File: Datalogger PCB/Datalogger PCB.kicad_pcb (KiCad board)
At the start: 4 copper layers, 42.2 x 101.8 mm, 51 parts, among them J1 Conn_01x02_Pin, M1 Motor_Servo, M2 Motor_Servo, M3 Motor_Servo, M4 Motor_Servo, U1 Teensy4.1, U2 BNO055, U3 LPS25HB, U4 AMS1117-5.0, U5 NRF24L01_Breakout, U6 VN5E160STR-E, U7 VN5E160STR-E, U8 VN5E160STR-E, U9 VN5E160STR-E

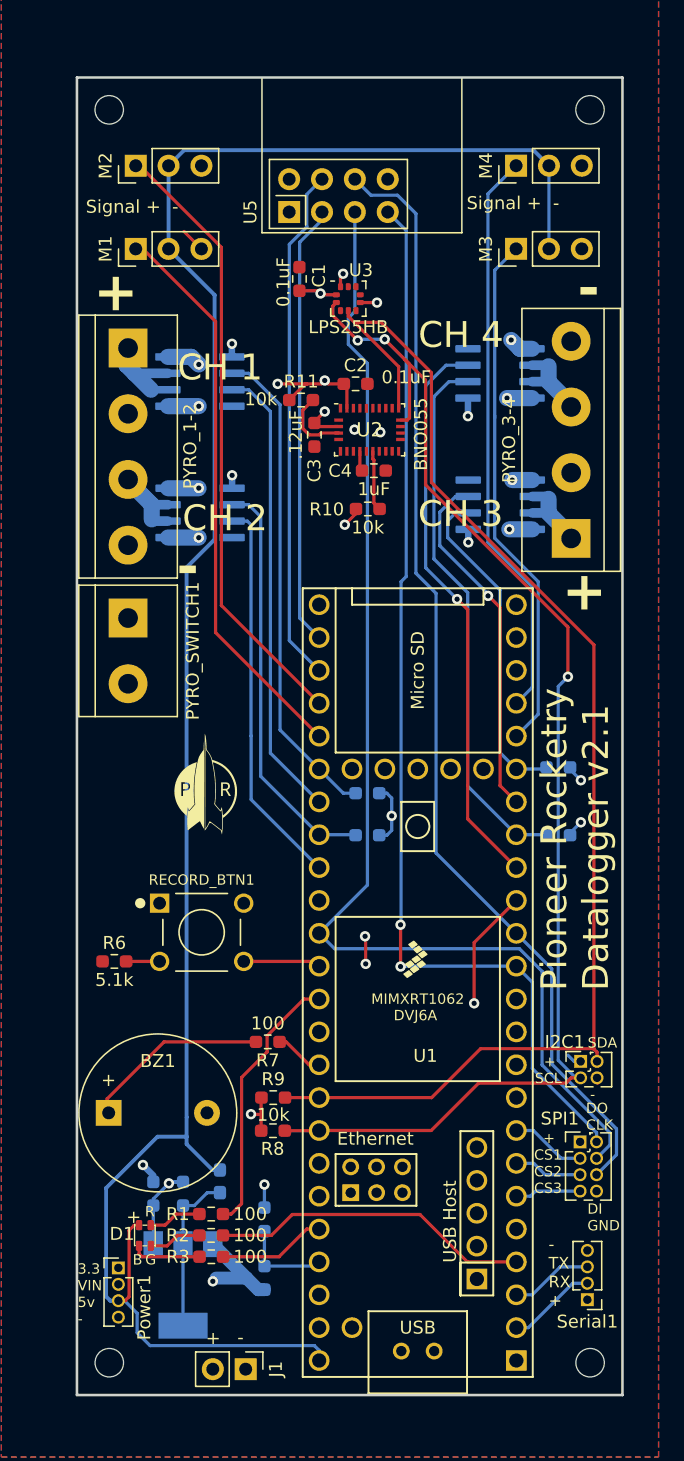
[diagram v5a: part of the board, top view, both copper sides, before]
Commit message: Made connectors bigger and removed unused radio connector
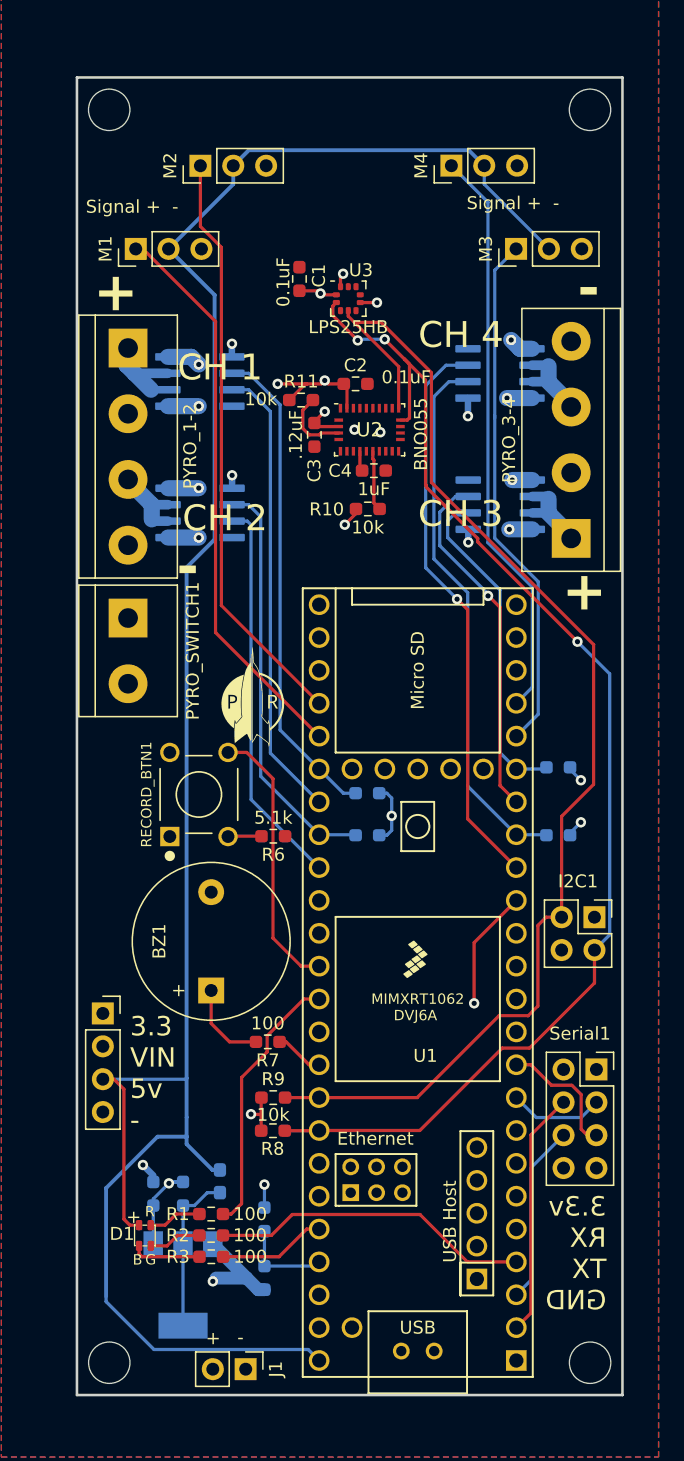
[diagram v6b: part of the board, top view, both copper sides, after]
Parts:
- removed SPI1: Conn_02x04_Counter_Clockwise, Connector_PinHeader_1.27mm:PinHeader_2x04_P1.27mm_Vertical
- removed U5: NRF24L01_Breakout, RF_Module:nRF24L01_Breakout
- H1, H2, H3, H4: footprint MountingHole:MountingHole_2.2mm_M2 -> MountingHole:MountingHole_3.2mm_M3
- I2C1: footprint Connector_PinHeader_1.27mm:PinHeader_2x02_P1.27mm_Vertical -> Connector_PinSocket_2.54mm:PinSocket_2x02_P2.54mm_Vertical
- Power1: footprint Connector_PinHeader_1.27mm:PinHeader_1x04_P1.27mm_Vertical -> Connector_PinSocket_2.54mm:PinSocket_1x04_P2.54mm_Vertical
- Serial1: value Conn_01x04_Pin -> Conn_02x04_Odd_Even; footprint Connector_PinHeader_1.27mm:PinHeader_1x04_P1.27mm_Vertical -> Connector_PinSocket_2.54mm:PinSocket_2x04_P2.54mm_Vertical
- moved Power1 19.7 mm to (139.6, 114.5)
- moved Serial1 17.8 mm to (177.7, 118.9), turned to 0 degrees
- moved R6 15.6 mm to (152.7, 100.8), turned to 180 degrees
- moved BZ1 12.3 mm to (147.9, 112.8), turned to 90 degrees
- moved I2C1 11.2 mm to (177.6, 107.1)
- moved RECORD_BTN1 10.7 mm to (147.0, 97.6), turned to 90 degrees
- moved G*** 7.68 mm to (151.1, 89.9)
- moved M2 5.00 mm to (147.1, 49.0)
- moved M4 5.00 mm to (166.5, 49.0)
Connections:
- Serial1 pad 2: /RX -> +3.3V
- Serial1 pad 3: /TX -> /RX2
- Serial1 pad 4: GND -> /RX
- U1 pad 10: unconnected-(U1-8_TX2_IN1-Pad10) -> /TX2
- U1 pad 26: /RADIO_CE -> unconnected-(U1-34_RX8-Pad26)
- U1 pad 27: /RADIO_CS -> unconnected-(U1-35_TX8-Pad27)
- U1 pad 9: unconnected-(U1-7_RX2_OUT1A-Pad9) -> /RX2
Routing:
- net /CLK: track 93.6 -> 0.00 mm
- net /DI: track 87.2 -> 0.00 mm
- net /DO: track 84.2 -> 0.00 mm, vias 2 -> 0
- net /RADIO_CS: track 40.0 -> 0.00 mm
- net /RADIO_CE: track 34.2 -> 0.00 mm
- net /RECORD_BTN: track 6.63 -> 21.8 mm
- net /RX: track 6.91 -> 18.9 mm
- net /TX2: track 0.00 -> 10.0 mm
- net Net-(BZ1--): track 14.4 -> 6.60 mm
- net /RX2: track 0.00 -> 7.79 mm
- net /TX: track 6.38 -> 13.8 mm
- net +5V: track 161.4 -> 167.2 mm
- net /EXTERNAL_CS1: track 5.82 -> 0.00 mm
- net /EXTERNAL_CS2: track 5.29 -> 0.00 mm
- net /EXTERNAL_CS3: track 5.09 -> 0.00 mm
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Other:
- board text added: "3.3v RX TX GND"
- board text removed: "+ CS1 CS2 CS3"
- board text removed: "+ SCL"
- board text removed: "- TX RX +"
- board text removed: "DI GND"
- board text removed: "DO CLK"
- board text removed: "SDA"

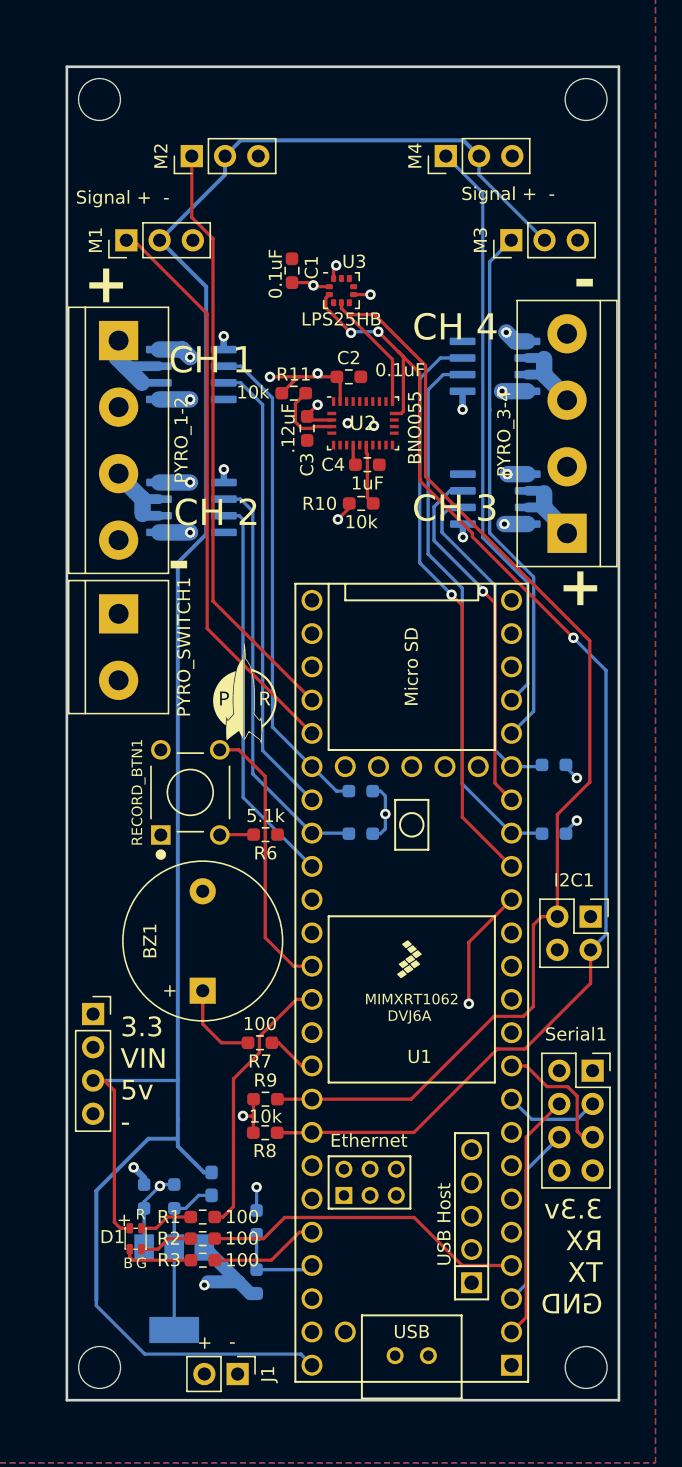
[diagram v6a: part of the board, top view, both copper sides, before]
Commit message: Removed Diode and replaced with jumper
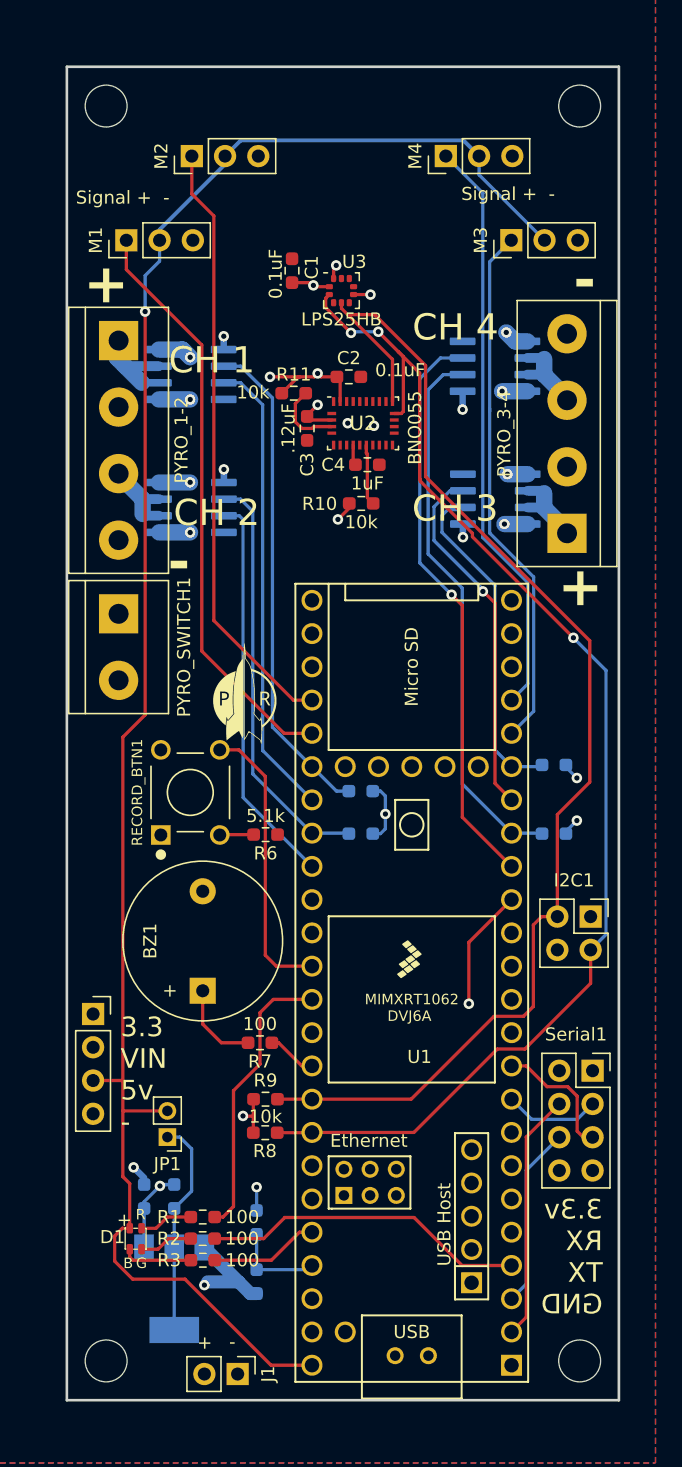
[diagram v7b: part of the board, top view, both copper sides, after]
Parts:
- removed D2: D, Diode_SMD:D_0603_1608Metric_Pad1.05x0.95mm_HandSolder
- added JP1: Jumper_2_Open, Connector_PinHeader_2.00mm:PinHeader_1x02_P2.00mm_Vertical, F.Cu at (145.2, 123.9)
- moved H1 0.71 mm to (140.5, 45.2)
- moved H3 0.71 mm to (176.7, 141.0)
- moved H4 0.71 mm to (140.5, 141.0)
- moved H2 0.70 mm to (176.7, 45.2)
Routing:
- net +5V: track 167.2 -> 141.6 mm, vias 0 -> 1
- net Net-(JP1-A): track 13.0 -> 17.1 mm
- net /RGB-R: track 20.9 -> 21.9 mm
- net /SERVO_1: track 43.9 -> 44.8 mm
- net /SERVO_2: track 45.4 -> 46.2 mm
- net /RECORD_BTN: track 21.8 -> 22.5 mm
